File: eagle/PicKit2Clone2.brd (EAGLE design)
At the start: 74 x 42.4 mm, 51 parts, among them IC1 PIC18F2550_28DIP, Q1 BC548, Q2 BC548, Q3 BC548, Q4 BC558A, Q5 BC548, Q6 BC558A, Q7 BC558A, Q8 BC558A, Q9 20MHz

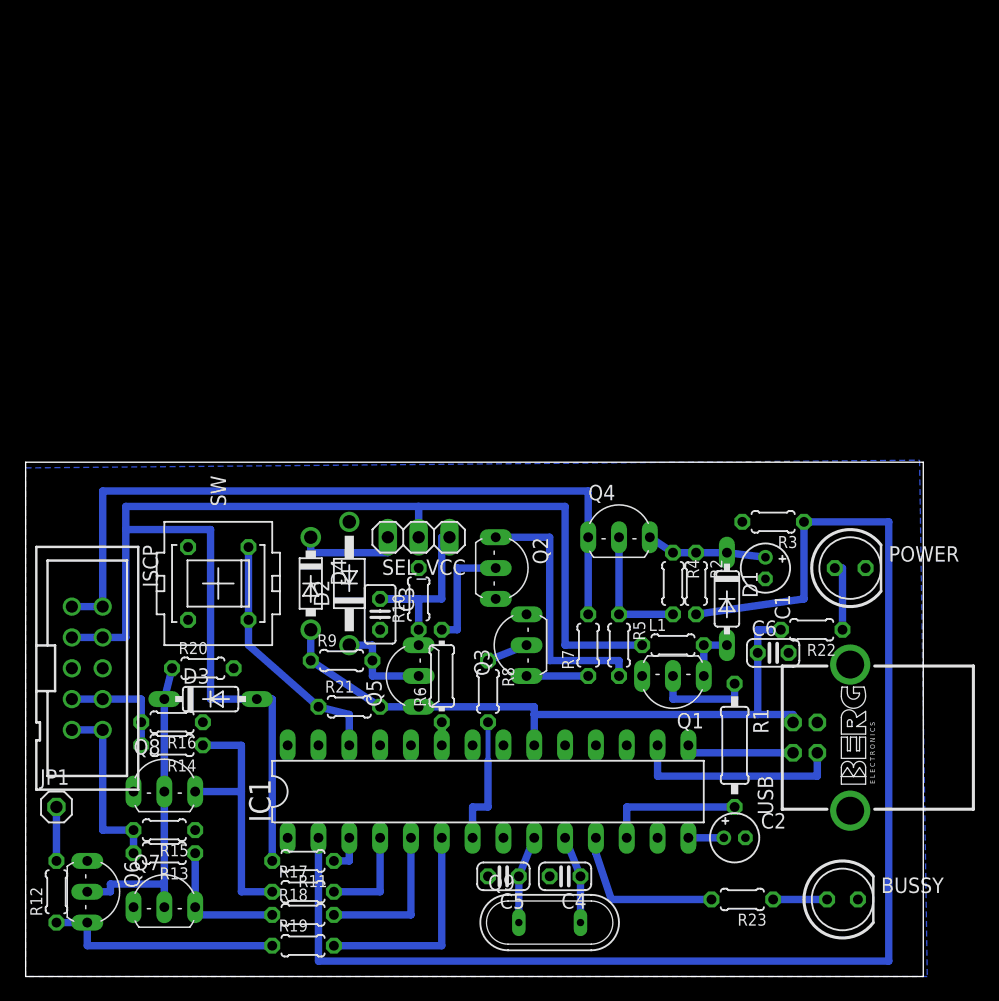
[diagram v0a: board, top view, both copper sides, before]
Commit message: Placa de 5x5. Doble capa no es util
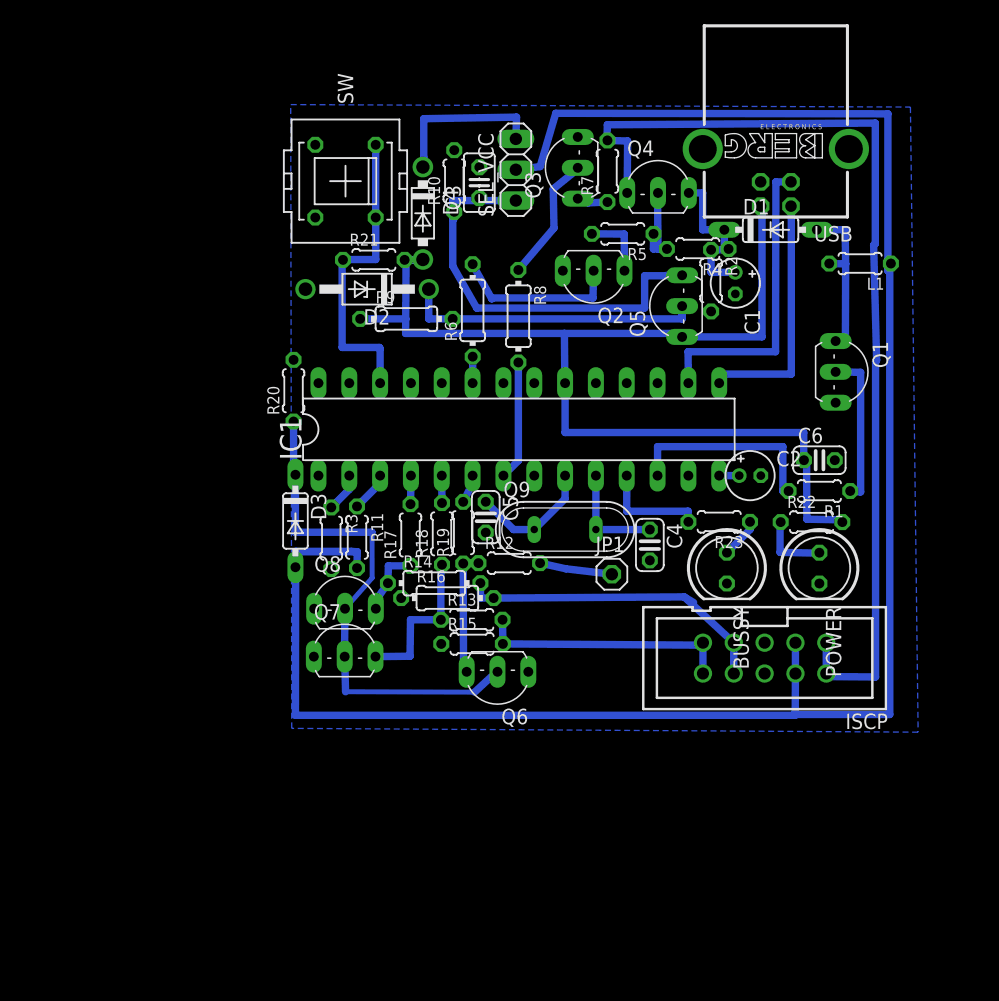
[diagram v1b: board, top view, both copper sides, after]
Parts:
- R1: device resistor:0207/10 -> resistor:0204/5
- R14, R16, R8, R9: device resistor:0204/5 -> resistor:0204/7
- moved ISCP 55.8 mm to (86.9, 29.4), turned to 180 degrees
- moved JP1 49.6 mm to (74.3, 36.3)
- moved USB 48.9 mm to (87.9, 71.4), turned to 180 degrees
- moved R12 46.1 mm to (65.9, 37.2), turned to 0 degrees
- moved Q3 39.6 mm to (70.3, 69.8)
- moved R7 39.1 mm to (74.0, 69.5)
- moved Q5 37.4 mm to (78.9, 58.4)
- moved R21 36.9 mm to (54.7, 62.2)
- moved Q6 36.6 mm to (64.9, 27.0), turned to 180 degrees
- moved R19 36.5 mm to (62.1, 39.7), turned to 90 degrees
- moved C3 36.5 mm to (63.4, 68.6), turned to 90 degrees
- moved R3 36.4 mm to (51.2, 39.3), turned to 270 degrees
- moved L1 35.0 mm to (94.8, 61.9), turned to 180 degrees
- moved SW 34.8 mm to (52.4, 68.7)
- moved R10 34.6 mm to (61.4, 68.7)
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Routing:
- net VPP_FB: track 115.7 -> 3.24 mm
- net VDD_TGT: track 111.1 -> 165.8 mm
- net +5V_USB: track 56.2 -> 90.3 mm
- net VDD_3.3V: track 17.8 -> 38.2 mm
- net ISCP_VPP: track 62.2 -> 82.0 mm
- net N$16: track 9.53 -> 27.0 mm
- net N$5: track 8.26 -> 25.4 mm
- net N$20: track 26.7 -> 42.8 mm
- net N$14: track 21.6 -> 5.66 mm
- net N$6: track 21.6 -> 5.68 mm
- net AUX: track 17.8 -> 2.35 mm
- net D-: track 9.24 -> 20.6 mm
- net ISCP_CLK: track 12.7 -> 2.26 mm
- net N$1: track 4.44 -> 13.8 mm
- net N$12: track 19.7 -> 10.4 mm
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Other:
- board outline removed

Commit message: mejora de 5x5
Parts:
- USB: value PN61729-S -> (none); device con-berg:PN61729-S -> con-berg:PN61729
- moved C3 2.91 mm to (63.4, 65.7), turned to 270 degrees
- moved R10 2.21 mm to (61.1, 66.5)
- moved JP1 1.77 mm to (76.0, 36.9), turned to 180 degrees
- moved Q4 1.46 mm to (78.2, 67.6)
- moved R8 1.38 mm to (67.8, 58.4)
- moved C2 1.22 mm to (86.7, 43.7), turned to 270 degrees
- moved C4 1.19 mm to (77.4, 39.9), turned to 90 degrees
- moved R5 1.19 mm to (74.6, 63.4)
- moved R6 1.12 mm to (64.0, 57.8)
- moved IC1 1.04 mm to (67.7, 48.4)
- moved R20 0.98 mm to (49.1, 51.5)
- moved D3 0.93 mm to (49.1, 40.3)
- moved C5 0.88 mm to (63.9, 40.1)
- moved R22 0.43 mm to (90.4, 40.7)
- moved SW 0.38 mm to (52.4, 68.3)
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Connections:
- net GND: no longer USB.S1, USB.S2
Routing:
- net N$11: track 13.4 -> 9.90 mm
- net VDD_3.3V: track 38.2 -> 40.8 mm
- net VDD_FB: track 3.33 -> 5.50 mm
- net N$3: track 13.0 -> 10.8 mm
- net N$4: track 7.02 -> 4.92 mm
- net OSC1: track 10.4 -> 12.4 mm
- net N$21: track 5.99 -> 7.63 mm
- net SW: track 25.5 -> 26.9 mm
- net N$6: track 5.68 -> 4.35 mm
- net N$8: track 10.8 -> 9.45 mm
- net D+: track 25.0 -> 23.8 mm
- net D-: track 20.6 -> 19.5 mm
- net ISCP_VPP: track 82.0 -> 80.9 mm
- net VPP_PUMP: track 16.8 -> 15.7 mm
- net N$10: track 1.65 -> 2.46 mm
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
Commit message: cambios menores
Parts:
- D2: value 1N4728 -> 1N4731
- R11: value 10K -> 4K7
- R7: value 10K -> 100
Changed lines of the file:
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@@
 <?xml version="1.0" encoding="utf-8"?>
 <!DOCTYPE eagle SYSTEM "eagle.dtd">
-<eagle version="7.4.0">
+<eagle version="6.5.0">
 <drawing>
 <settings>
@@
 <layer number="23" name="tOrigins" color="15" fill="1" visible="yes" active="yes"/>
 <layer number="24" name="bOrigins" color="15" fill="1" visible="yes" active="yes"/>
-<layer number="25" name="tNames" color="7" fill="1" visible="no" active="yes"/>
-<layer number="26" name="bNames" color="7" fill="1" visible="no" active="yes"/>
-<layer number="27" name="tValues" color="7" fill="1" visible="no" active="yes"/>
-<layer number="28" name="bValues" color="7" fill="1" visible="no" active="yes"/>
+<layer number="25" name="tNames" color="7" fill="1" visible="yes" active="yes"/>
+<layer number="26" name="bNames" color="7" fill="1" visible="yes" active="yes"/>
+<layer number="27" name="tValues" color="7" fill="1" visible="yes" active="yes"/>
+<layer number="28" name="bValues" color="7" fill="1" visible="yes" active="yes"/>
 <layer number="29" name="tStop" color="7" fill="3" visible="no" active="yes"/>
 <layer number="30" name="bStop" color="7" fill="6" visible="no" active="yes"/>
@@
 <pass name="Default">
 <param name="RoutingGrid" value="50mil"/>
-<param name="AutoGrid" value="1"/>
-<param name="Efforts" value="0"/>
-<param name="TopRouterVariant" value="1"/>
 <param name="tpViaShape" value="round"/>
-<param name="PrefDir.1" value="a"/>
+<param name="PrefDir.1" value="|"/>
 <param name="PrefDir.2" value="0"/>
 <param name="PrefDir.3" value="0"/>
@@
 <param name="PrefDir.14" value="0"/>
 <param name="PrefDir.15" value="0"/>
-<param name="PrefDir.16" value="a"/>
+<param name="PrefDir.16" value="-"/>
 <param name="cfVia" value="8"/>
 <param name="cfNonPref" value="5"/>
@@
 <element name="Q2" library="transistor-npn" package="TO92-EBC" value="BC548" x="72.796146875" y="59.80870625" rot="R180"/>
 <element name="R6" library="resistor" package="0204/7" value="10K" x="63.96846875" y="57.81750625" rot="R90"/>
-<element name="R7" library="resistor" package="0204/5" value="10K" x="73.97695" y="69.530471875" rot="R90"/>
+<element name="R7" library="resistor" package="0204/5" value="100" x="73.97695" y="69.530471875" rot="R90"/>
 <element name="R8" library="resistor" package="0204/7" value="10K" x="67.77398125" y="58.3691375" rot="R270"/>
 <element name="Q3" library="transistor-npn" package="TO92-EBC" value="BC548" x="70.260178125" y="69.81259375" rot="R90"/>
@@
 <element name="C3" library="rcl" package="C025-025X050" value="100n" x="63.39395625" y="65.67723125" rot="R270"/>
 <element name="C2" library="rcl" package="E1,8-4" value="1uF" x="86.68134375" y="43.691303125" rot="R270"/>
-<element name="D2" library="diode" package="DO41Z10" value="1N4728" x="54.1746125" y="59.814325" rot="R180"/>
+<element name="D2" library="diode" package="DO41Z10" value="1N4731" x="54.1746125" y="59.814325" rot="R180"/>
 <element name="D4" library="diode" package="DO41-7.6" value="1N5817-T" x="58.76741875" y="66.066865625" rot="R270"/>
-<element name="R11" library="resistor" package="0204/5" value="10K" x="53.34" y="39.37" rot="R270"/>
+<element name="R11" library="resistor" package="0204/5" value="4K7" x="53.34" y="39.37" rot="R270"/>
 <element name="ISCP" library="con-3m" package="PAK100/2500-10" value="2510-" x="86.927034375" y="29.411659375" rot="R180">
 <attribute name="OC_NEWARK" value="46F4725" x="86.927034375" y="29.411659375" size="1.778" layer="27" rot="R180" display="off"/>
